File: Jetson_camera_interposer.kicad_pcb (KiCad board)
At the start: 6 copper layers, 82.1 x 75 mm, 39 parts, among them J1 QSH-060-01-L-D-A, J2 QTH-060-01-L-D-A, J21 Conn_01x01, J22 Conn_01x01, J23 Conn_01x01, J24 Conn_01x01, J25 Conn_01x01, J26 Conn_01x01, J3 Conn_01x01, J4 Conn_01x01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

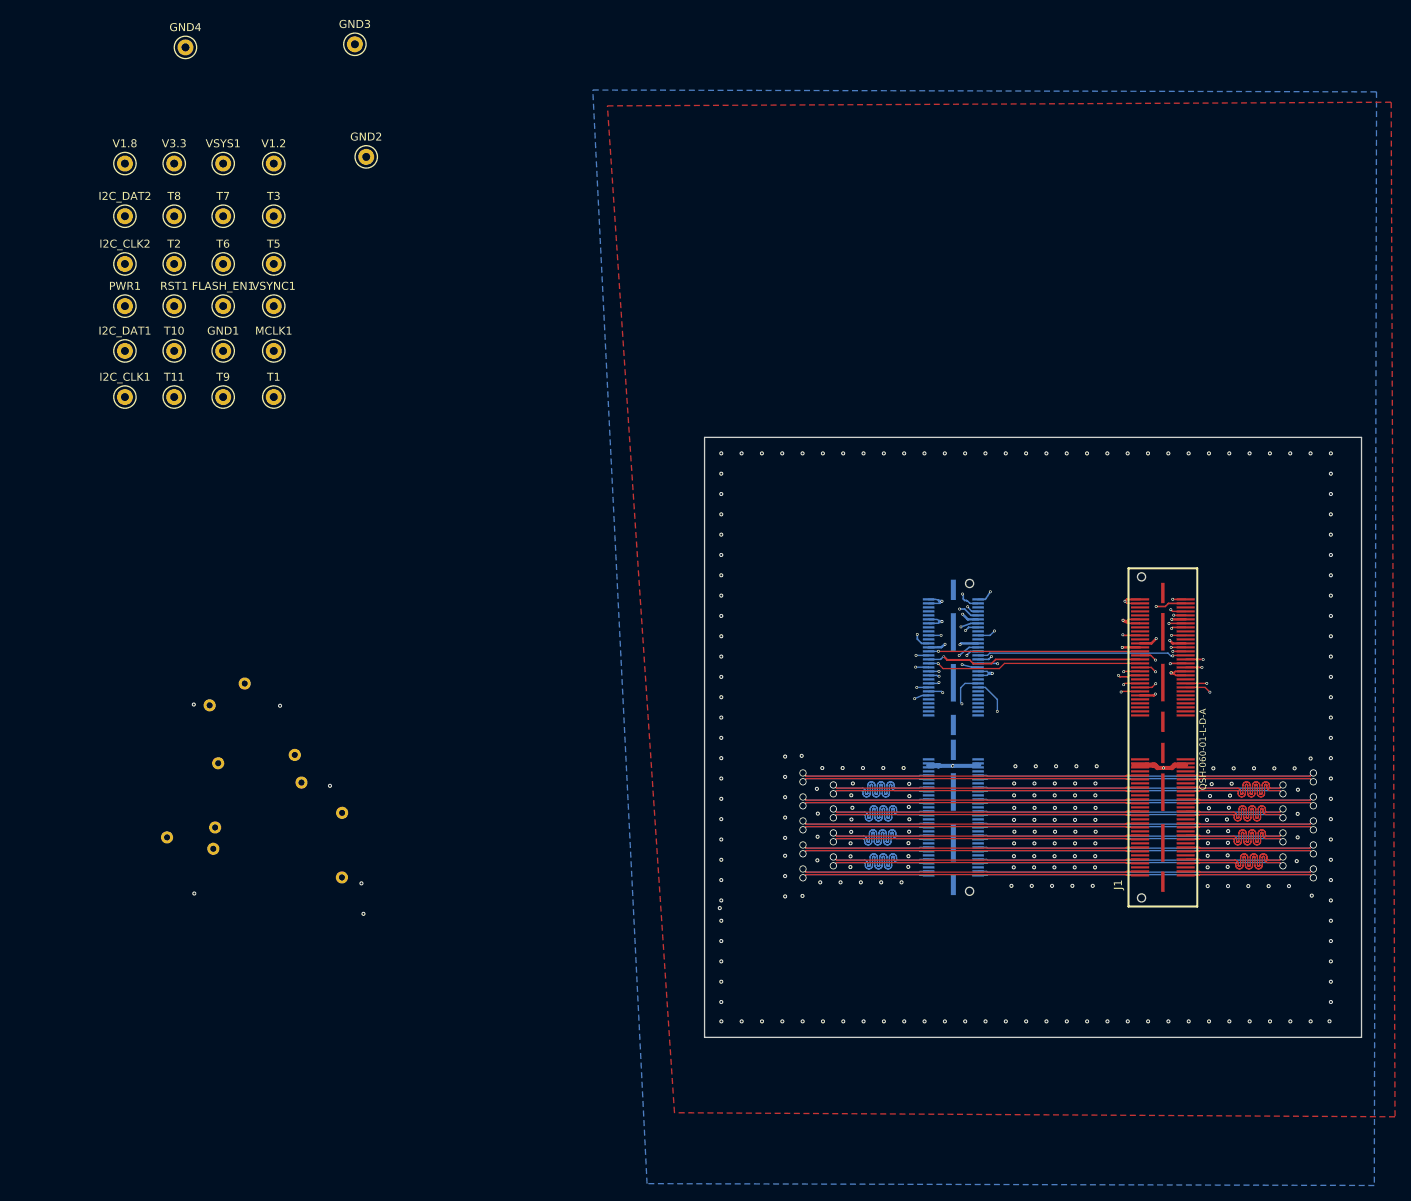
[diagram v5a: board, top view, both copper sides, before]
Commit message: Added debug connector
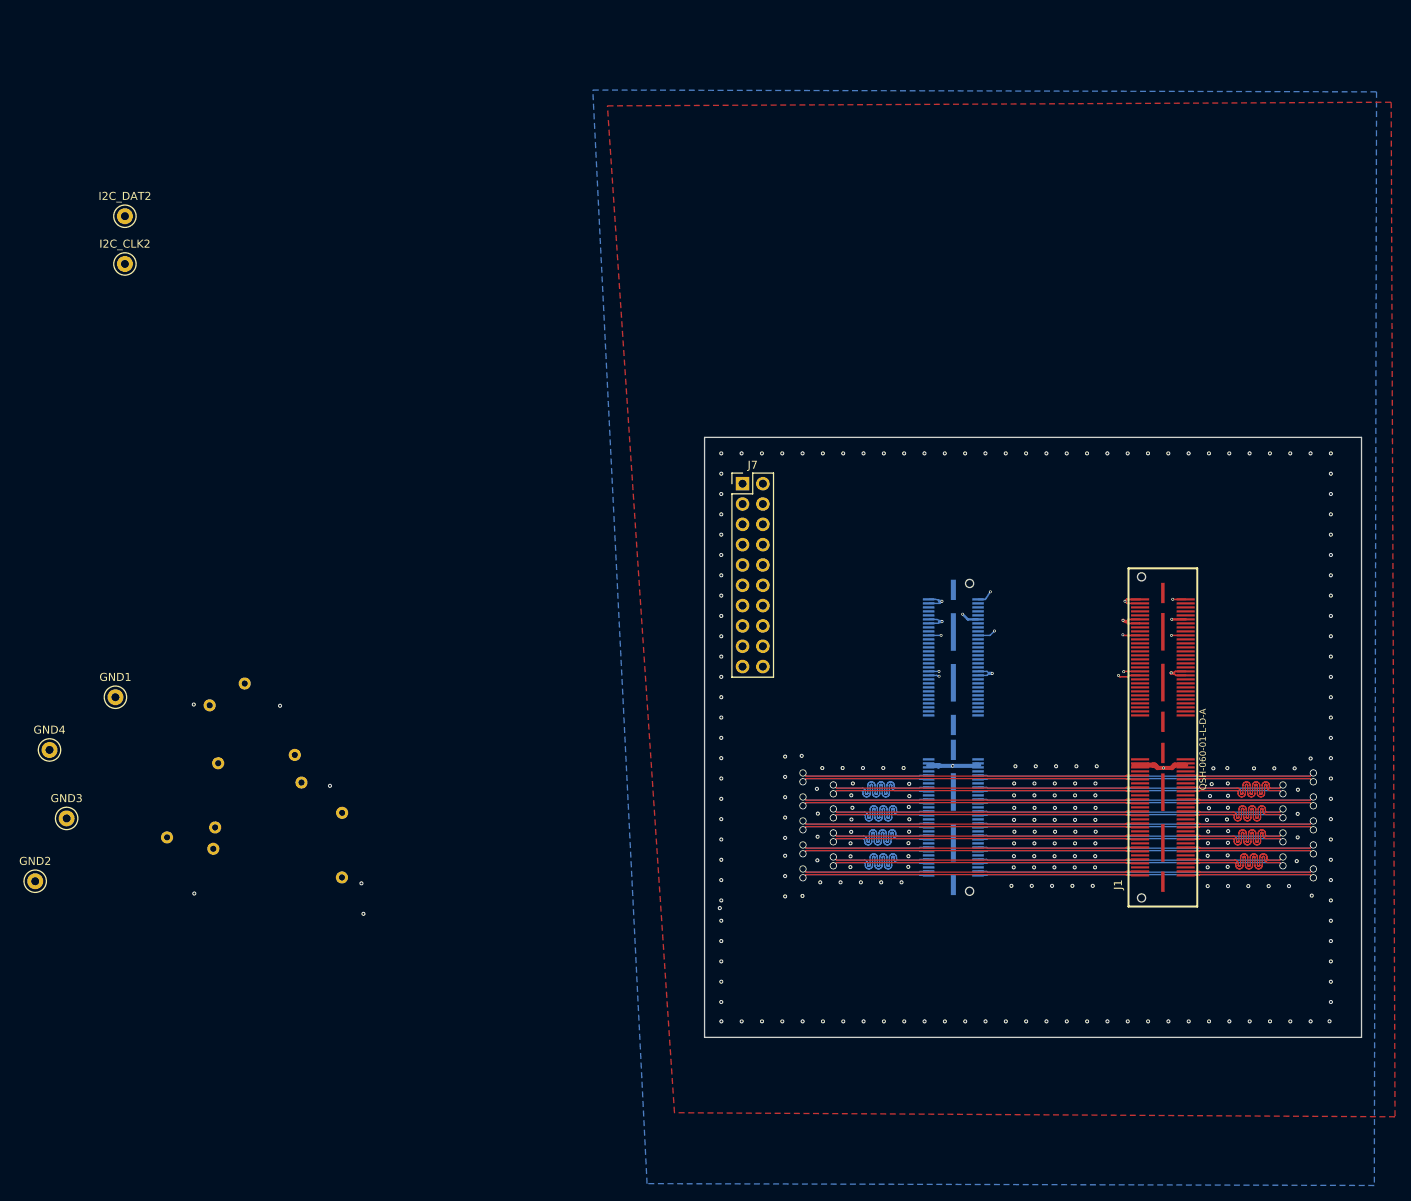
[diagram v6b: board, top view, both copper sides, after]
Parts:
- removed FLASH_EN1, I2C_CLK1, I2C_DAT1, MCLK1, PWR1, RST1, T1, T10, T11, T2, T3, T5, T6, T7, T8, T9, V1.2, V1.8, V3.3, VSYNC1, VSYS1: TestP, TX2_Footprints:test_point
- added J7: Conn_02x10_Odd_Even, Pin_Headers:Pin_Header_Straight_2x10_Pitch2.54mm, F.Cu at (93.7, 71.8)
- moved GND3 103.3 mm to (9.16, 113.6)
- moved GND2 99.6 mm to (5.23, 121.5)
- moved GND4 89.4 mm to (7.02, 105.1)
- moved GND1 45.3 mm to (15.3, 98.5)
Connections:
- J1 pad 101: /JETSON_1V2 -> /JETSON_1V2_J
- J1 pad 102: /JETSON_1V8 -> /JETSON_1V8_J
- J1 pad 108: /VDD_3V3 -> /VDD_3V3_J
- J1 pad 109: /VDD_IR -> /VDD_IR_J
- J1 pad 110: /VDD_3V3 -> /VDD_3V3_J
- J1 pad 118: /VDD_SYS -> /VDD_SYS_J
- J1 pad 120: /VDD_SYS -> /VDD_SYS_J
- J1 pad 55: /DVDD_CAM_LV -> /DVDD_CAM_LV_J
- J1 pad 56: /DVDD_CAM_LV -> /DVDD_CAM_LV_J
- J1 pad 57: /DVDD_CAM_LV -> /DVDD_CAM_LV_J
- J1 pad 58: /DVDD_CAM_LV -> /DVDD_CAM_LV_J
- J1 pad 81: /VDD_CAM_FQ_HV_CAM -> /VDD_CAM_FQ_HV_CAM_J
- J1 pad 82: /AVDD_CAM -> /AVDD_CAM_J
- J1 pad 83: /VDD_CAM_FQ_HV_CAM -> /VDD_CAM_FQ_HV_CAM_J
- J1 pad 84: /VDD_AF -> /VDD_AF_J
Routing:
- net /I2C_CAM_DAT: track 38.8 -> 0.00 mm, vias 2 -> 0
- net /I2C_CAM_CLK: track 35.4 -> 0.00 mm, vias 2 -> 0
- net /CAM1_RST_L: track 35.3 -> 0.00 mm, vias 2 -> 0
- net /CAM_VSYNC: track 34.9 -> 0.00 mm, vias 2 -> 0
- net /CAM2_RST: track 34.8 -> 0.00 mm, vias 2 -> 0
- net /CAM_AF_PWDN: track 34.3 -> 0.00 mm, vias 2 -> 0
- net /I2S3_CLK: track 34.2 -> 0.00 mm, vias 2 -> 0
- net /I2S3_SDIN: track 33.8 -> 0.00 mm, vias 2 -> 0
- net /IR_READY: track 32.1 -> 0.00 mm, vias 2 -> 0
- net /CAM0_RST: track 31.6 -> 0.00 mm, vias 2 -> 0
- net /CAM_INTR: track 31.4 -> 0.00 mm, vias 2 -> 0
- net /CAM_FLASH_EN: track 31.0 -> 0.00 mm, vias 2 -> 0
- net /CAM_I2C2_SDA: track 30.7 -> 0.00 mm, vias 2 -> 0
- net /I2C_GP0_DAT_1V8: track 30.3 -> 0.00 mm, vias 2 -> 0
- net /I2C_GP0_CLK_1V8: track 29.9 -> 0.00 mm, vias 2 -> 0
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
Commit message: routing
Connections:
- J7 pad 1: /VDD_SYS -> /VDD_SYS_J
- J7 pad 2: /VDD_SYS_J -> /VDD_SYS
- J7 pad 3: /VDD_IR -> /VDD_IR_J
- J7 pad 4: /VDD_IR_J -> /VDD_IR
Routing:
- net /VDD_IR_J: track 0.00 -> 67.9 mm, vias 0 -> 1
- net /VDD_SYS_J: track 0.00 -> 55.6 mm, vias 0 -> 1
- net /VDD_3V3: track 30.5 -> 11.5 mm, vias 2 -> 1
- net /VDD_3V3_J: track 0.00 -> 4.14 mm, vias 0 -> 1
- net /VDD_IR: track 30.3 -> 32.3 mm, vias 2 -> 1
- net /VDD_SYS: track 30.6 -> 31.0 mm, vias 2 -> 1

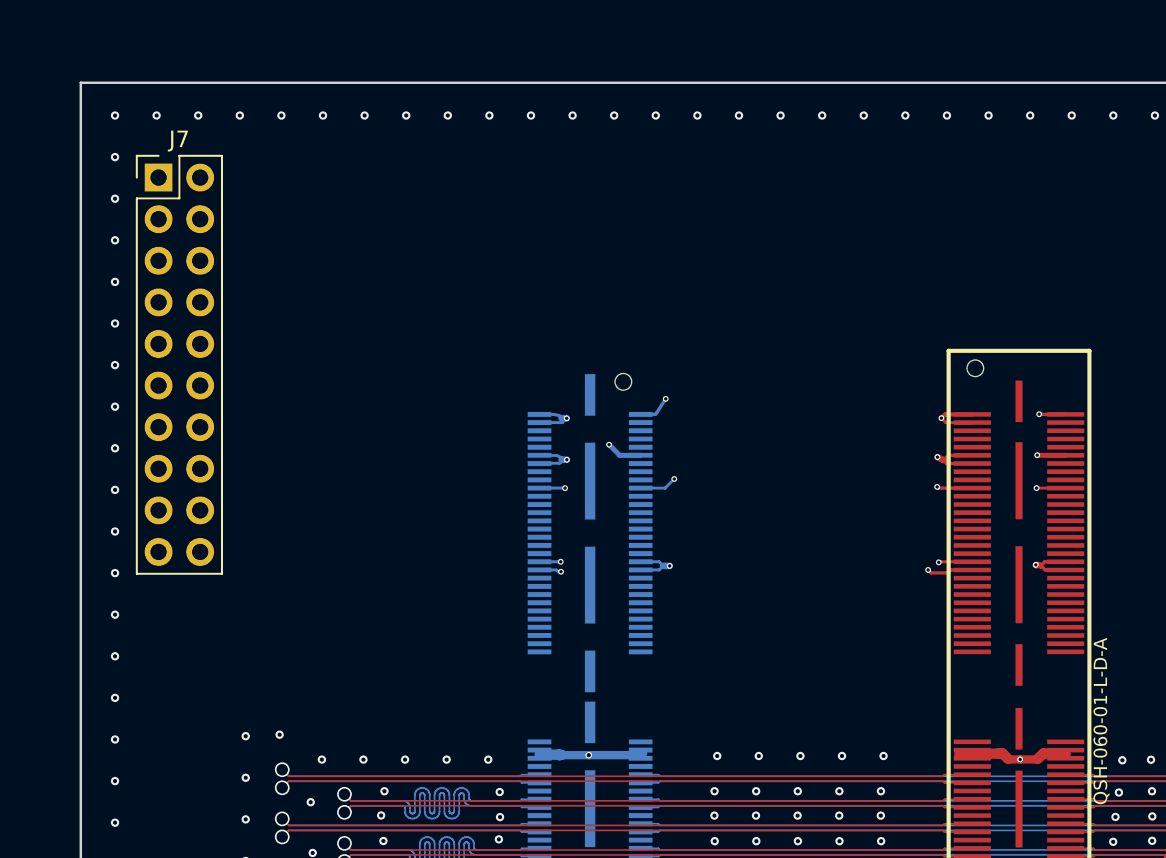
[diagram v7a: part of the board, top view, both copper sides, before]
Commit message: good, before changing footprint
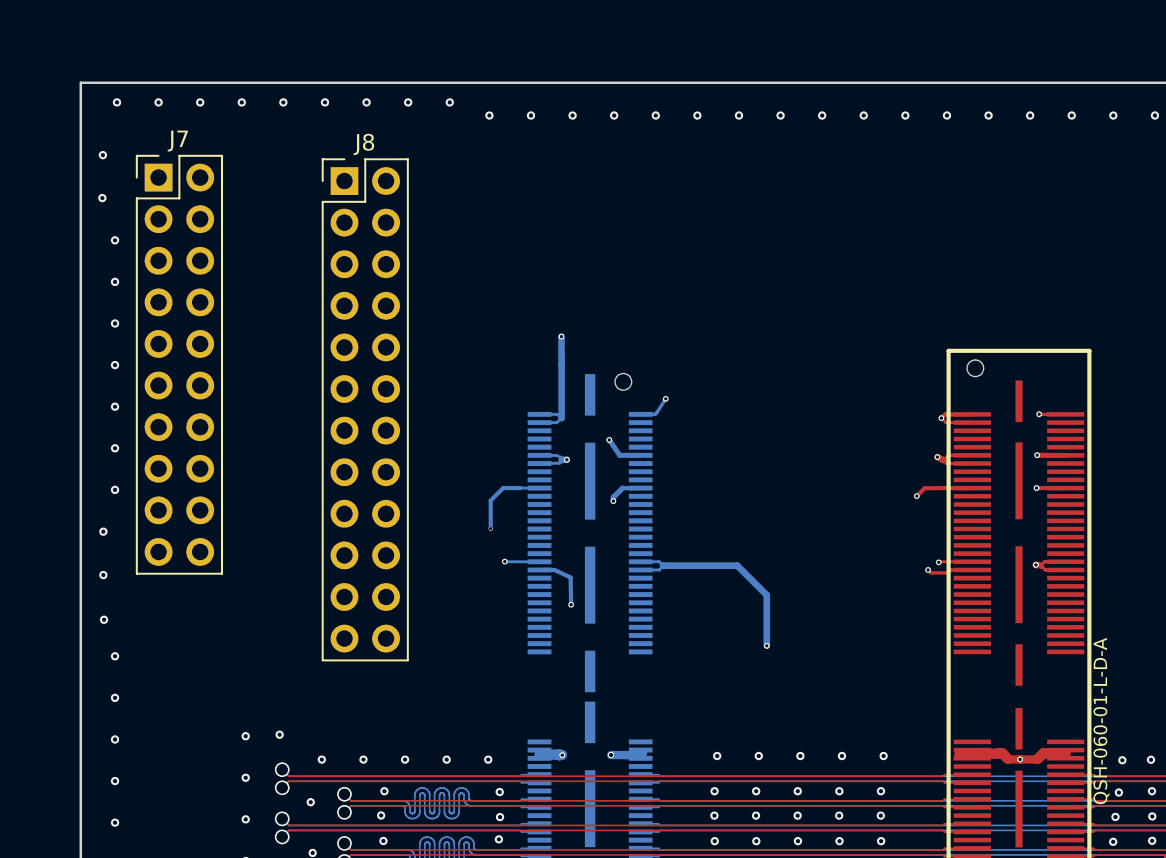
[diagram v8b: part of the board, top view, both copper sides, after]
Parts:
- added J8: Conn_02x30_Odd_Even, Pin_Headers:Pin_Header_Straight_2x12_Pitch2.54mm, F.Cu at (105.0, 72.0)
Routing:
- net /VDD_CAM_FQ_HV_CAM: track 30.5 -> 99.4 mm, vias 2 -> 1
- net /DVDD_CAM_LV_J: track 0.00 -> 66.0 mm, vias 0 -> 1
- net /VDD_CAM_FQ_HV_CAM_J: track 0.00 -> 65.8 mm, vias 0 -> 1
- net /JETSON_1V2_J: track 0.00 -> 57.5 mm, vias 0 -> 1
- net /AVDD_CAM_J: track 0.00 -> 54.9 mm, vias 0 -> 1
- net /VDD_AF_J: track 0.00 -> 52.4 mm, vias 0 -> 1
- net /VDD_3V3_J: track 4.14 -> 56.6 mm
- net /JETSON_1V8_J: track 0.00 -> 51.9 mm, vias 0 -> 1
- net /VDD_3V3: track 11.5 -> 36.1 mm
- net /AVDD_CAM: track 27.4 -> 41.0 mm, vias 2 -> 1
- net /VDD_SYS: track 31.0 -> 40.7 mm
- net /JETSON_1V2: track 26.6 -> 34.9 mm, vias 2 -> 1
- net /VDD_IR_J: track 67.9 -> 73.7 mm
- net /VDD_SYS_J: track 55.6 -> 60.6 mm
- net /JETSON_1V8: track 26.5 -> 31.0 mm, vias 2 -> 1
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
